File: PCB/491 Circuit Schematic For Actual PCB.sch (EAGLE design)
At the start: 27 parts, among them IC1 7812T

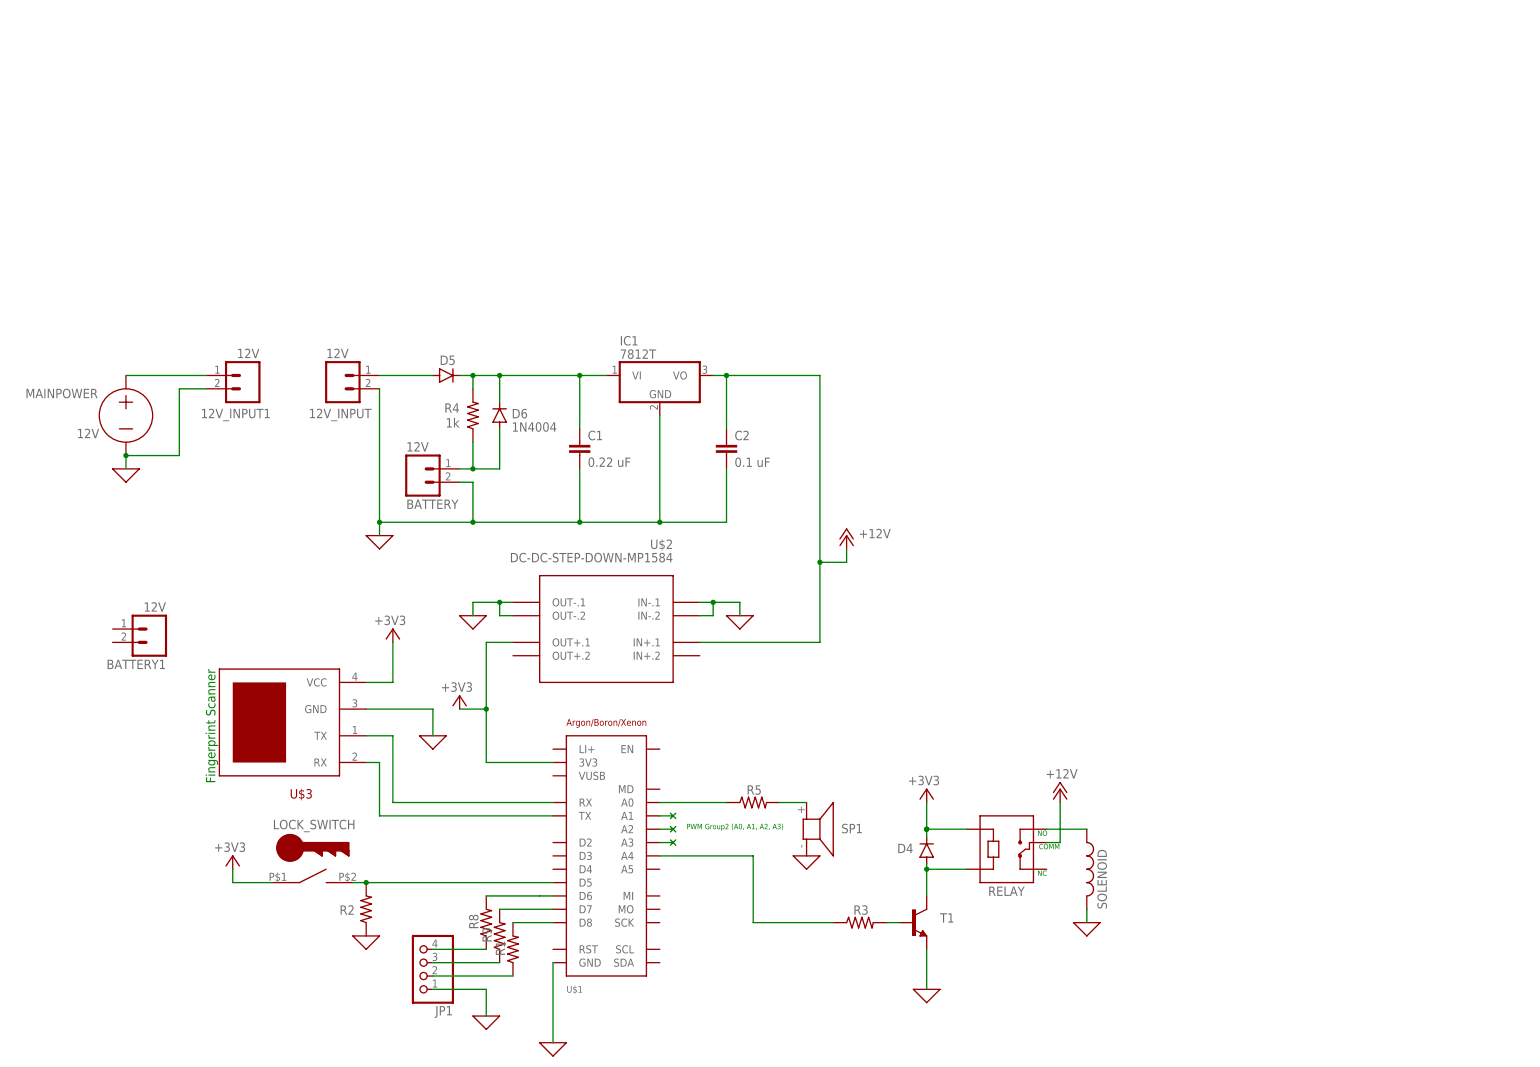
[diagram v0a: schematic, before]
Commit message: Edited Schematic, started layout
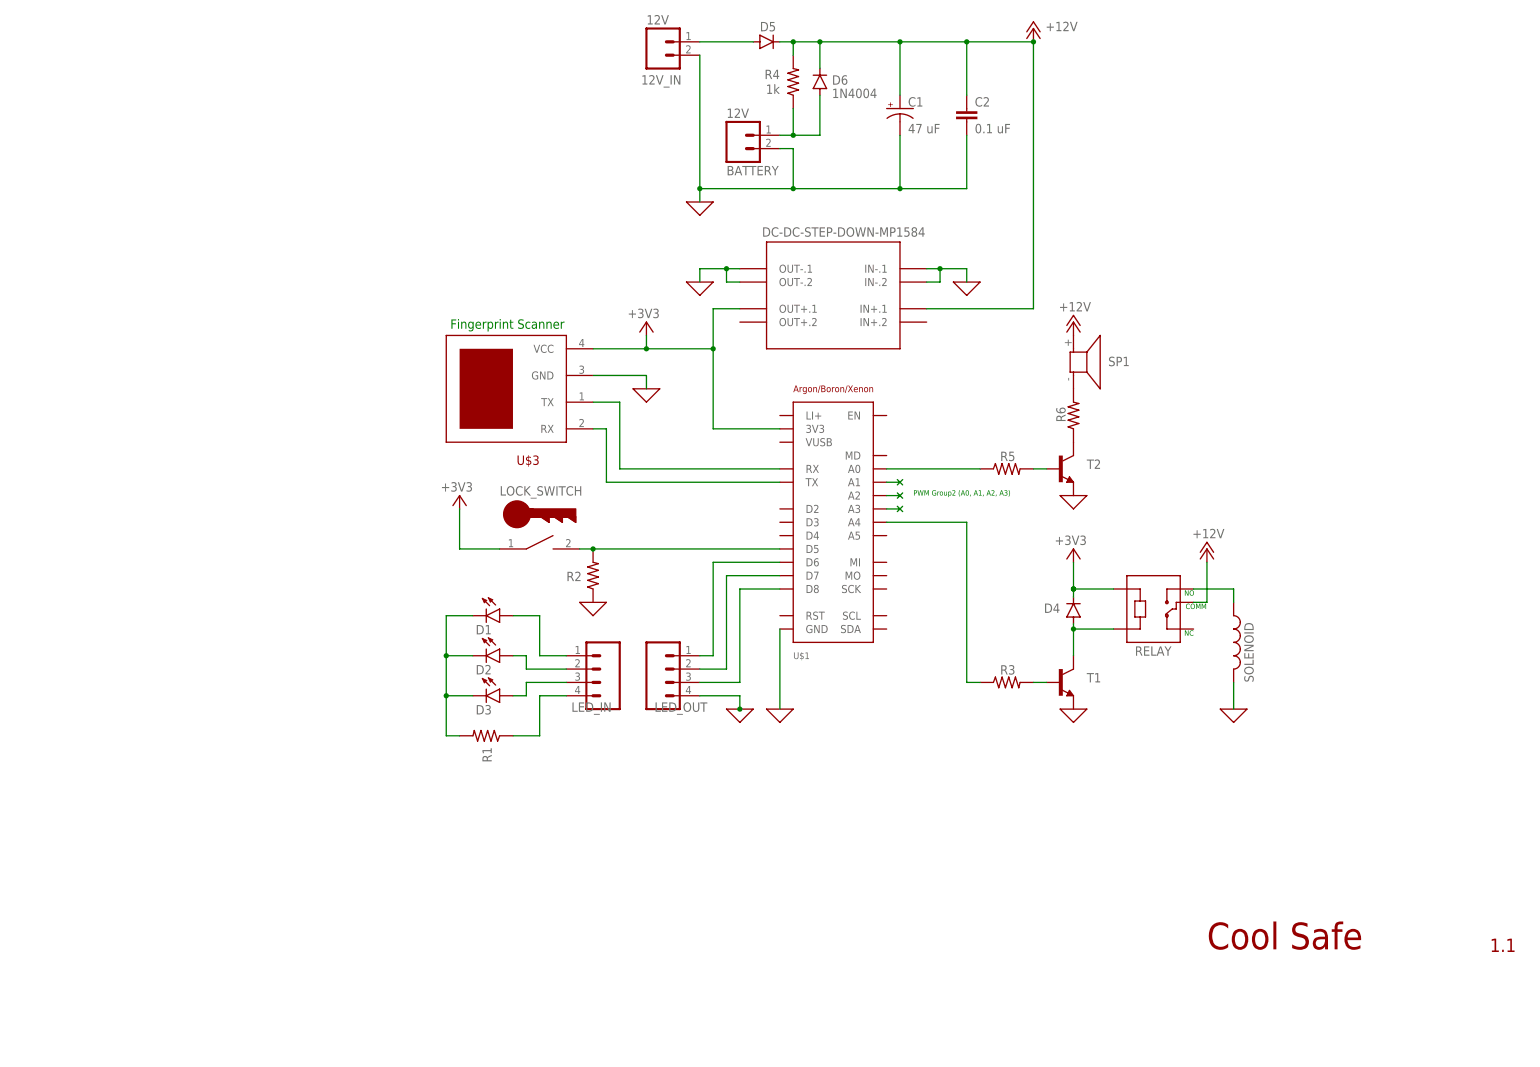
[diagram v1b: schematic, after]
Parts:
- removed 12V_INPUT, 12V_INPUT1, BATTERY1: 12V, con-amp-quick:M02
- removed IC1: 7812T, linear:7812T
- removed JP1: (no value), cool_safe_lib:PINHD-1X4
- removed MAINPOWER: 12V, ngspice-simulation:VOLTAGE
- removed R8, R9: (no value), rcl:R-US_0204/7
- added 12V_IN: 12V, con-amp-quick:M02
- added D1, D2, D3: U57X32, led:U57X32
- added LED_IN, LED_OUT: (no value), con-amp-quick:M04
- added R6: (no value), rcl:R-US_0204/7
- added T2: (no value), transistor:-NPN-TO92
- C1: value 0.22 uF -> 47 uF; device capacitor-wima:C2.5/5 -> rcl:CPOL-USE2.5-6
- LOCK_SWITCH: value LOCK_SWITCH -> LOCK_SWITCH02P; device cool_safe_lib:LOCK_SWITCH -> cool_safe_lib:LOCK_SWITCH02P
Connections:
- removed net FPS: SP1.2
- net +12V: now also C1.+, D5.C, D6.C, R4.2, SP1.1; no longer IC1.VO
- net 0: now also 12V_IN.2, C1.-, LED_OUT.4, T2.E; no longer 12V_INPUT.2, 12V_INPUT1.2, C1.2, IC1.GND, JP1.1, MAINPOWER.-
- net N$1: now also D3.A, LED_IN.3; no longer 12V_INPUT1.1, MAINPOWER.+
- net N$10: now also D1.C, D2.C, D3.C, R1.2; no longer R8.2
- net N$15: now also R6.1, T2.C; no longer C1.1, D5.C, D6.C, IC1.VI, R4.2
- net N$2: now also T2.B; no longer SP1.1
- net N$29: now also 12V_IN.1; no longer 12V_INPUT.1
- net N$3: now also D2.A, LED_IN.2; no longer U$1.D6
- net N$30: now also LED_IN.4, R1.1; no longer R9.2
- net N$31: now also R6.2, SP1.2; no longer R1.2, U$1.D8
- net N$5: now also D1.A, LED_IN.1; no longer U$1.D7
- net N$6: now also LED_OUT.1, U$1.D6; no longer JP1.4, R8.1
- net N$7: now also LED_OUT.2, U$1.D7; no longer JP1.3, R9.1
- net N$8: now also LED_OUT.3, U$1.D8; no longer JP1.2, R1.1
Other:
- note added: "1.1"
- note added: "Cool Safe"
- moved on the sheet: BATTERY, C2, D4, D5, D6, LOCK_SWITCH, R1, R2, R3, R4, R5, RELAY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

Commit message: Update to PCB
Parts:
- removed 12V_IN, BATTERY: 12V, con-amp-quick:M02
- removed D1, D2, D3: U57X32, led:U57X32
- removed L2: SOLENOID, rcl:L-US0207/5V
- removed LED_IN, LED_OUT: (no value), con-amp-quick:M04
- removed R1: (no value), rcl:R-US_0204/7
- added JP1: (no value), pinhead:PINHD-1X4/90
- added SOLENOID: (no value), SparkFun-Connectors:JST_2MM_MALE
- added X1, X2: 1751248, con-phoenix-350:1751248
- LOCK_SWITCH: value LOCK_SWITCH02P -> LOCK_SWITCHSCREW_TERMINAL; device cool_safe_lib:LOCK_SWITCH02P -> cool_safe_lib:LOCK_SWITCHSCREW_TERMINAL
- R2: device rcl:R-US_0204/7 -> rcl:R-US_0207/10
- RELAY: value SRD-05VDC-SL-C -> ZF112; device SRD-05VDC-SL-C:SRD-05VDC-SL-C -> relay:ZF112
- U$3: value FPS -> FPSQWIIC; device cool_safe_lib:FPS -> cool_safe_lib:FPSQWIIC
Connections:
- removed net N$10: D1.C, D2.C, D3.C, R1.2
- removed net N$14: BATTERY.1, D6.A, R4.1
- removed net N$19: U$1.A1
- removed net N$22: U$1.A2
- removed net N$25: U$1.A3
- removed net N$3: D2.A, LED_IN.2
- removed net N$30: LED_IN.4, R1.1
- removed net N$5: D1.A, LED_IN.1
- net +12V: now also RELAY2.P, U$2.IN+.2; no longer RELAY.COM
- net +3V3: now also RELAY1.1, U$2.OUT+.2; no longer RELAY.A1
- net 0: now also JP1.1, SOLENOID.+, X1-1.K, X2-1.K; no longer 12V_IN.2, BATTERY.2, L2.2, LED_OUT.4
- net N$1: now also D6.A, R4.1, X2-2.K; no longer D3.A, LED_IN.3
- net N$11: now also RELAY1.2; no longer RELAY.A2
- net N$13: now also RELAY2.S, SOLENOID.-; no longer L2.1, RELAY.NO
- net N$29: now also X1-2.K; no longer 12V_IN.1
- net N$6: now also JP1.4; no longer LED_OUT.1
- net N$7: now also JP1.3; no longer LED_OUT.2
- net N$8: now also JP1.2; no longer LED_OUT.3
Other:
- note added: "12V IN"
- note added: "BATTERY"
- moved on the sheet: D4
